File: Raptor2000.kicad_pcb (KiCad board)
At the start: 4 copper layers, 63.5 x 63.5 mm, 35 parts, among them J1 Wuerth_7499010121A, J4 Micro_SD_Card, SW1 SW_Push, U1 TM4C1294NCPDTGOOD, U2 ET60T-02-24-02-X-RTX-GP, U4 ESP-12E, U5 IS42S16400J-xC, Y1 Crystal_GND24

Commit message: updates
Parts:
- removed C17, C18: C_Small, Capacitor_SMD:C_0603_1608Metric
- removed J1: Wuerth_7499010121A, Connector_RJ:RJ45_Wuerth_7499010121A_Horizontal
- removed R3, R36, R4: R_Small, Resistor_SMD:R_0603_1608Metric
- removed SW1: SW_Push, Button_Switch_SMD:SW_SPST_EVPBF
- removed U4: ESP-12E, RF_Module:ESP-12E
- added R5: R_Small, Resistor_SMD:R_0603_1608Metric, F.Cu at (159.3, 94.5)
- U2: footprint Exodus_Connectors:ET60T-02-24-02-X-RTX-GP-HS -> ET60T-02-24-02-X-RTX-GP:ET60T-02-24-02-X-RTX-GP
- moved J4 52.3 mm to (135.9, 71.6), turned to 180 degrees
- moved D1 52.1 mm to (183.6, 66.8)
- moved R30 48.8 mm to (183.6, 68.6), turned to 0 degrees
- moved C1 35.3 mm to (145.7, 111.4), turned to 0 degrees
- moved C7 34.9 mm to (137.4, 104.9), turned to 270 degrees
- moved C2 33.5 mm to (149.4, 111.4), turned to 0 degrees
- moved C9 33.0 mm to (139.2, 104.9), turned to 270 degrees
- moved C6 32.5 mm to (153.7, 111.5), turned to 0 degrees
- moved C38 32.2 mm to (170.1, 70.7), turned to 0 degrees
- moved C5 32.0 mm to (137.4, 101.6), turned to 90 degrees
- moved C35 30.4 mm to (177.0, 81.8), turned to 270 degrees
- moved C10 30.0 mm to (139.2, 101.6), turned to 270 degrees
- moved C36 28.7 mm to (165.5, 70.7), turned to 0 degrees
- moved C8 23.1 mm to (158.5, 104.8), turned to 90 degrees
- moved C33 22.6 mm to (171.8, 90.3), turned to 0 degrees
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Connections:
- D1 pad 2: +BATT -> +3V3
- U1 pad 102: Net-(U1-Pad102) -> (no net)
- U1 pad 105: Net-(U1-Pad105) -> (no net)
- U1 pad 106: Net-(U1-Pad106) -> (no net)
- U1 pad 107: Net-(U1-Pad107) -> (no net)
- U1 pad 108: Net-(U1-Pad108) -> (no net)
- U1 pad 109: Net-(U1-Pad109) -> (no net)
- U1 pad 11: Net-(U1-Pad11) -> (no net)
- U1 pad 110: Net-(U1-Pad110) -> (no net)
- U1 pad 111: Net-(U1-Pad111) -> (no net)
- U1 pad 112: Net-(U1-Pad112) -> (no net)
- U1 pad 116: Net-(U1-Pad116) -> (no net)
- U1 pad 117: Net-(U1-Pad117) -> (no net)
- U1 pad 118: Net-(U1-Pad118) -> (no net)
- U1 pad 119: Net-(U1-Pad119) -> (no net)
- U1 pad 12: Net-(U1-Pad12) -> (no net)
- U1 pad 120: Net-(U1-Pad120) -> (no net)
- U1 pad 121: Net-(U1-Pad121) -> (no net)
- U1 pad 123: Net-(U1-Pad123) -> (no net)
- U1 pad 124: Net-(U1-Pad124) -> (no net)
- U1 pad 125: Net-(U1-Pad125) -> (no net)
- U1 pad 126: Net-(U1-Pad126) -> (no net)
- U1 pad 13: Net-(U1-Pad13) -> (no net)
- U1 pad 14: Net-(U1-Pad14) -> (no net)
- U1 pad 15: Net-(U1-Pad15) -> (no net)
- U1 pad 27: Net-(U1-Pad27) -> (no net)
- U1 pad 29: Net-(U1-Pad29) -> (no net)
- U1 pad 30: Net-(U1-Pad30) -> (no net)
- U1 pad 31: Net-(U1-Pad31) -> /Connectors/~ENABLE
- U1 pad 32: Net-(U1-Pad32) -> /Connectors/~INHIBIT
- U1 pad 33: Net-(U1-Pad33) -> (no net)
- U1 pad 34: Net-(U1-Pad34) -> (no net)
- U1 pad 35: Net-(U1-Pad35) -> (no net)
- U1 pad 36: Net-(U1-Pad36) -> (no net)
- U1 pad 37: Net-(U1-Pad37) -> (no net)
- U1 pad 38: Net-(U1-Pad38) -> (no net)
- U1 pad 42: /Connectors/ETH_LED0 -> (no net)
- U1 pad 43: Net-(U1-Pad43) -> (no net)
- U1 pad 44: Net-(U1-Pad44) -> (no net)
- U1 pad 45: Net-(U1-Pad45) -> (no net)
- U1 pad 46: /Connectors/ETH_LED1 -> (no net)
- U1 pad 5: Net-(U1-Pad5) -> (no net)
- U1 pad 6: Net-(U1-Pad6) -> (no net)
- U1 pad 60: Net-(U1-Pad60) -> (no net)
- U1 pad 61: Net-(U1-Pad61) -> (no net)
- U1 pad 63: Net-(U1-Pad63) -> (no net)
- U1 pad 64: Net-(U1-Pad64) -> (no net)
- U1 pad 65: Net-(U1-Pad65) -> (no net)
- U1 pad 66: Net-(U1-Pad66) -> (no net)
- U1 pad 67: Net-(U1-Pad67) -> (no net)
- U1 pad 71: Net-(U1-Pad71) -> (no net)
- U1 pad 72: Net-(U1-Pad72) -> (no net)
- U1 pad 73: Net-(U1-Pad73) -> (no net)
- U1 pad 74: Net-(U1-Pad74) -> (no net)
- U1 pad 85: Net-(U1-Pad85) -> (no net)
- U1 pad 86: Net-(U1-Pad86) -> (no net)
- U1 pad 91: Net-(U1-Pad91) -> (no net)
- U1 pad 95: /TM4C129/USB_ID -> (no net)
- U1 pad 96: Net-(U1-Pad96) -> (no net)
- U2 pad 1: Net-(U2-Pad1) -> (no net)
- U2 pad 10: /Connectors/BOARD_SENSE -> (no net)
- U2 pad 11: /Connectors/~SYSRESET -> /JTAG_TDO
- U2 pad 12: Net-(U2-Pad12) -> /JTAG_TDI
- U2 pad 13: Net-(U2-Pad13) -> (no net)
- U2 pad 14: Net-(U2-Pad14) -> (no net)
- U2 pad 15: Net-(U2-Pad15) -> (no net)
- U2 pad 19: /JTAG_TDO -> /JTAG_TMS
- U2 pad 2: Net-(U2-Pad2) -> (no net)
- U2 pad 20: /JTAG_TDI -> /JTAG_TCK
- U2 pad 21: /JTAG_TMS -> /TM4C129/ETH_RXI_N
- U2 pad 22: /JTAG_TCK -> /TM4C129/ETH_RXI_P
- U2 pad 23: /Connectors/~JTAG_TRST -> /TM4C129/ETH_TXO_N
- U2 pad 24: Net-(U2-Pad24) -> /TM4C129/ETH_TXO_P
- U2 pad 3: Net-(U2-Pad3) -> (no net)
- U2 pad 4: Net-(U2-Pad4) -> (no net)
- U2 pad 5: Net-(U2-Pad5) -> (no net)
- U2 pad 6: Net-(U2-Pad6) -> (no net)
- U2 pad 7: Net-(U2-Pad7) -> (no net)
- U2 pad 9: Net-(U2-Pad9) -> (no net)
- U5 pad 40: Net-(U5-Pad40) -> (no net)
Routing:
- net /TM4C129/USB_D_N: track 0.00 -> 58.2 mm
- net /TM4C129/USB_D_P: track 0.00 -> 58.2 mm
- net /JTAG_TDO: track 0.00 -> 48.0 mm, vias 0 -> 1
- net /JTAG_TDI: track 0.00 -> 47.5 mm, vias 0 -> 1
- net /JTAG_TCK: track 0.00 -> 42.5 mm, vias 0 -> 1
- net /JTAG_TMS: track 0.00 -> 41.6 mm, vias 0 -> 1
- net /Connectors/SPI_SS: track 12.4 -> 53.7 mm
- net /Connectors/SPI_SCLK: track 14.4 -> 54.9 mm
- net /Connectors/SPI_MOSI: track 16.9 -> 52.2 mm
- net /Connectors/SPI_MISO: track 18.1 -> 51.1 mm
- net /Connectors/SPI_DAT2: track 14.6 -> 47.4 mm
- net /Connectors/SPI_DAT3: track 16.7 -> 46.7 mm
- net /TM4C129/ETH_TXO_P: track 0.00 -> 27.9 mm
- net /TM4C129/ETH_TXO_N: track 0.00 -> 27.5 mm
- net +BATT: track 0.00 -> 26.0 mm
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- added copper zone on In2.Cu, net +3V3
- removed copper zone on B.Cu, net +3V3
- removed copper zone on In2.Cu, net +BATT
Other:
- net class Default: clearance 0.2 -> 0.127; trace_width 0.25 -> 0.1778
- rule trace_clearance: 0.2 -> 0.127

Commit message: fixing some unnamed nets.
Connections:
- net Net-(C4-Pad2) renamed /TM4C129/OSC1_R
- net Net-(C5-Pad1) renamed /TM4C129/VDDC
- net Net-(D1-Pad1) renamed /PWR_LED_CATHODE
- net Net-(R2-Pad1) renamed /TM4C129/R_BIAS
- net Net-(R5-Pad2) renamed /TM4C129/RST

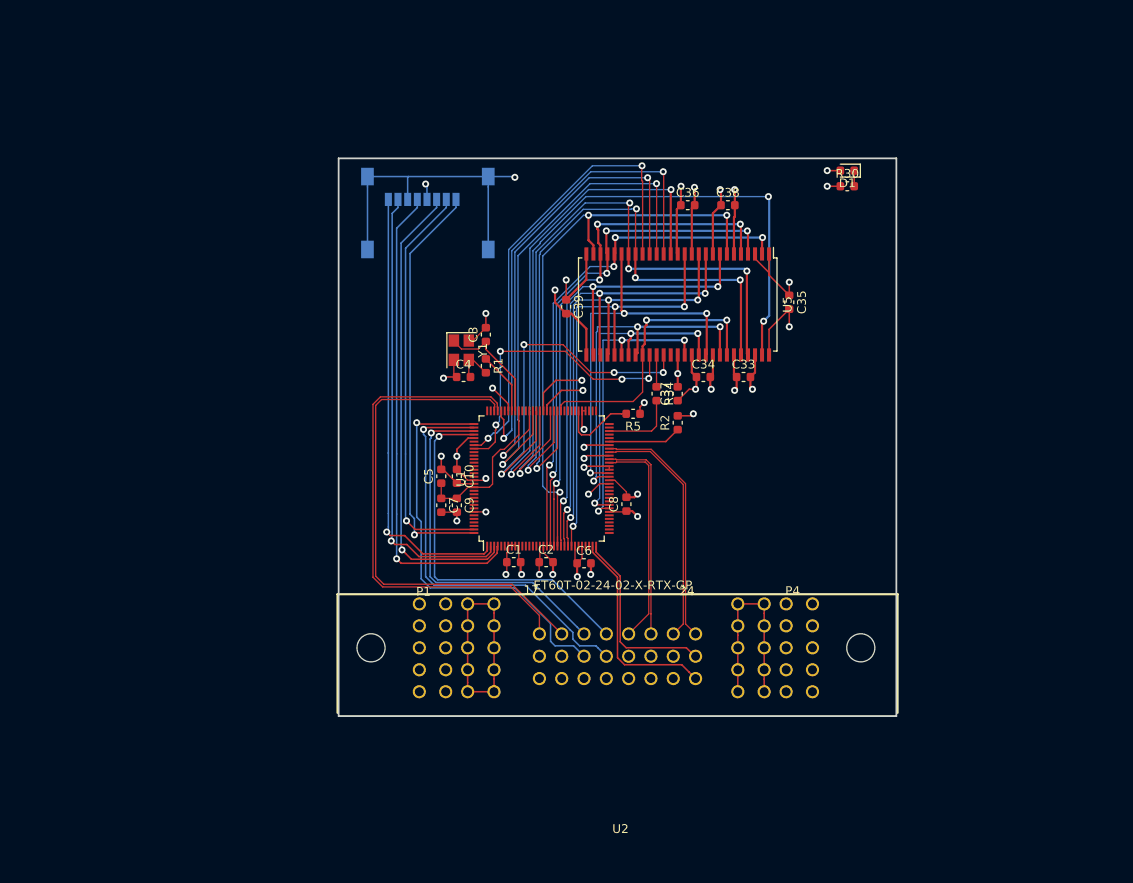
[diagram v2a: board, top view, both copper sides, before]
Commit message: regenerated netlist/annotations and refdeses. using new connector symbol.
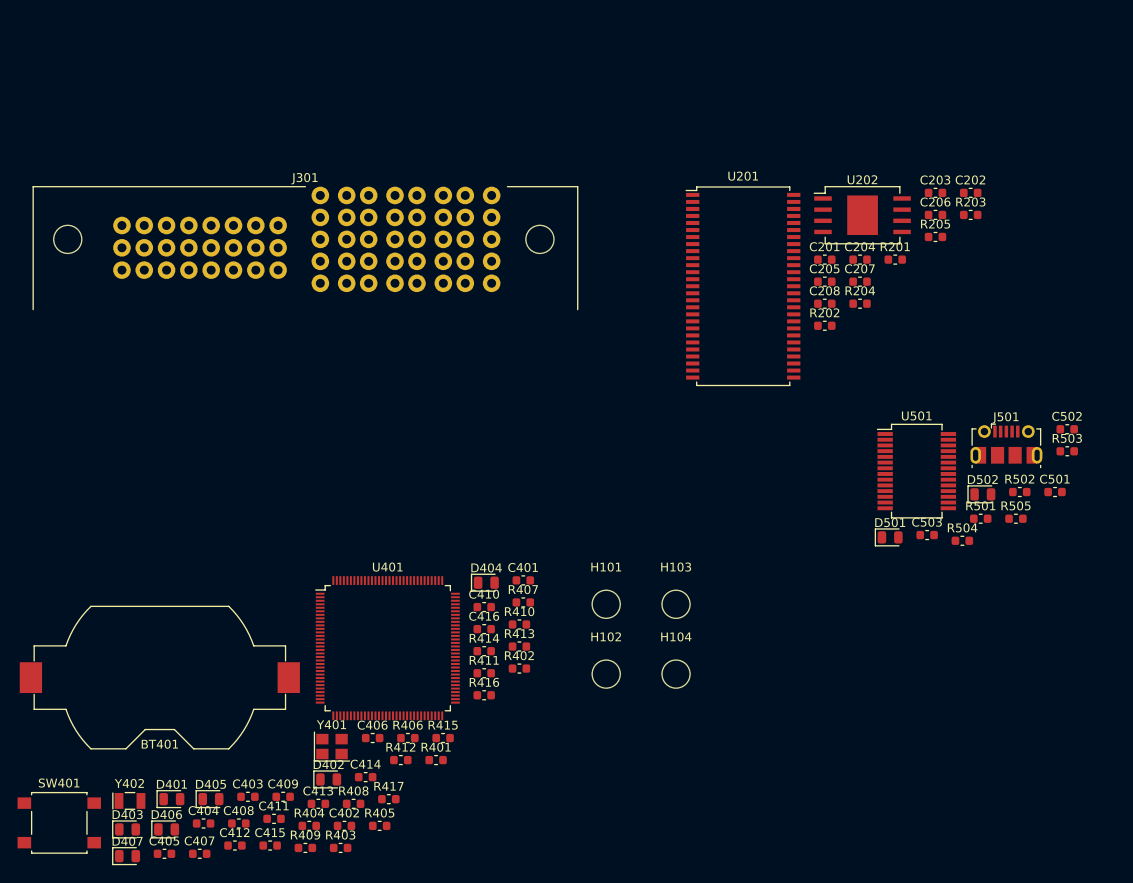
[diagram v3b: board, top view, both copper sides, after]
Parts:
- removed C1, C9: 2.2u, Capacitor_SMD:C_0603_1608Metric
- removed C10, C33, C34, C35, C36, C37, C38, C39, C7: C_Small, Capacitor_SMD:C_0603_1608Metric
- removed C2, C6, C8: 0.1u, Capacitor_SMD:C_0603_1608Metric
- removed C3, C4: 12p, Capacitor_SMD:C_0603_1608Metric
- removed C5: 1.0u, Capacitor_SMD:C_0603_1608Metric
- removed D1: LED, LED_SMD:LED_0603_1608Metric
- removed J4: Micro_SD_Card, Connector_Card:microSD_HC_Wuerth_693072010801
- removed R1: 2k, Resistor_SMD:R_0603_1608Metric
- removed R2: 4.87k 1%, Resistor_SMD:R_0603_1608Metric
- removed R30, R5: R_Small, Resistor_SMD:R_0603_1608Metric
- removed R34: 0, Resistor_SMD:R_0603_1608Metric
- removed U1: TM4C1294NCPDTGOOD, Package_QFP:TQFP-128_14x14mm_P0.4mm
- removed U2: ET60T-02-24-02-X-RTX-GP, ET60T-02-24-02-X-RTX-GP:ET60T-02-24-02-X-RTX-GP
- removed U5: IS42S16400J-xC, Package_SO:TSOP-II-54_22.2x10.16mm_P0.8mm
- removed Y1: Crystal_GND24, Crystal:Crystal_SMD_3225-4Pin_3.2x2.5mm
- added BT401: Battery_Cell, Battery:BatteryHolder_Keystone_1058_1x2032, F.Cu at (105.4, 124.5)
- added C201: 0.1u, Capacitor_SMD:C_0603_1608Metric, F.Cu at (181.1, 76.9)
- added C202: 0.1u, Capacitor_SMD:C_0603_1608Metric, F.Cu at (197.7, 69.3)
- added C203: 0.1u, Capacitor_SMD:C_0603_1608Metric, F.Cu at (193.7, 69.3)
- added C204: 0.1u, Capacitor_SMD:C_0603_1608Metric, F.Cu at (185.1, 76.9)
- added C205: 0.1u, Capacitor_SMD:C_0603_1608Metric, F.Cu at (181.1, 79.4)
- added C206: 0.1u, Capacitor_SMD:C_0603_1608Metric, F.Cu at (193.7, 71.8)
- added C207: 0.1u, Capacitor_SMD:C_0603_1608Metric, F.Cu at (185.1, 79.4)
- added C208: 0.1u, Capacitor_SMD:C_0603_1608Metric, F.Cu at (181.1, 82.0)
- added C401: 12p, Capacitor_SMD:C_0603_1608Metric, F.Cu at (146.8, 113.5)
- added C402: 12p, Capacitor_SMD:C_0603_1608Metric, F.Cu at (126.4, 141.4)
- added C403: 0.1u, Capacitor_SMD:C_0603_1608Metric, F.Cu at (115.4, 138.1)
- added C404: 1.0u, Capacitor_SMD:C_0603_1608Metric, F.Cu at (110.4, 141.1)
- added C405: 0.1u, Capacitor_SMD:C_0603_1608Metric, F.Cu at (105.9, 144.6)
- added C406: 0.1u, Capacitor_SMD:C_0603_1608Metric, F.Cu at (129.6, 131.4)
- added C407: 0.1u, Capacitor_SMD:C_0603_1608Metric, F.Cu at (109.9, 144.6)
- added C408: 2.2u, Capacitor_SMD:C_0603_1608Metric, F.Cu at (114.4, 141.1)
- added C409: 0.1u, Capacitor_SMD:C_0603_1608Metric, F.Cu at (119.4, 138.1)
- added C410: 0.1u, Capacitor_SMD:C_0603_1608Metric, F.Cu at (142.3, 116.5)
- added C411: 12p, Capacitor_SMD:C_0603_1608Metric, F.Cu at (118.4, 140.6)
- added C412: 12p, Capacitor_SMD:C_0603_1608Metric, F.Cu at (113.9, 143.6)
- added C413: 0.1u, Capacitor_SMD:C_0603_1608Metric, F.Cu at (123.4, 138.9)
- added C414: 0.1u, Capacitor_SMD:C_0603_1608Metric, F.Cu at (128.8, 135.9)
- added C415: 0.1u, Capacitor_SMD:C_0603_1608Metric, F.Cu at (117.9, 143.6)
- added C416: 2.2u, Capacitor_SMD:C_0603_1608Metric, F.Cu at (142.3, 119.0)
- added C501: 0.1u, Capacitor_SMD:C_0603_1608Metric, F.Cu at (207.3, 103.4)
- added C502: 100nF, Capacitor_SMD:C_0603_1608Metric, F.Cu at (208.7, 96.2)
- added C503: 3300pF, Capacitor_SMD:C_0603_1608Metric, F.Cu at (192.7, 108.3)
- added D401: LED, LED_SMD:LED_0805_2012Metric, F.Cu at (106.7, 138.4)
- added D402: LED, LED_SMD:LED_0805_2012Metric, F.Cu at (124.6, 136.1)
- added D403: LED, LED_SMD:LED_0805_2012Metric, F.Cu at (101.7, 141.8)
- added D404: LED, LED_SMD:LED_0805_2012Metric, F.Cu at (142.5, 113.7)
- added D405: LED, LED_SMD:LED_0805_2012Metric, F.Cu at (111.2, 138.4)
- added D406: LED, LED_SMD:LED_0805_2012Metric, F.Cu at (106.1, 141.8)
- added D407: LED, LED_SMD:LED_0805_2012Metric, F.Cu at (101.7, 144.9)
- added D501: LED, Diode_SMD:D_0805_2012Metric, F.Cu at (188.5, 108.6)
- added D502: LED, Diode_SMD:D_0805_2012Metric, F.Cu at (199.1, 103.7)
- added H101: MountingHole, MountingHole:MountingHole_3.2mm_M3, F.Cu at (156.2, 116.2)
- added H102: MountingHole, MountingHole:MountingHole_3.2mm_M3, F.Cu at (156.2, 124.1)
- added H103: MountingHole, MountingHole:MountingHole_3.2mm_M3, F.Cu at (164.1, 116.2)
- added H104: MountingHole, MountingHole:MountingHole_3.2mm_M3, F.Cu at (164.1, 124.1)
- added J301: ET60T-000-3-08-D04-x-R1-S-x, Exodus_Connectors:Conn_Samtec_ET60T-000-3-08-D-4-x-R1-S-x, F.Cu at (122.0, 74.6)
- added J501: USB_B_Micro, Connector_USB:USB_Micro-B_Molex-105017-0001, F.Cu at (201.8, 98.0)
- added R201: 0, Resistor_SMD:R_0603_1608Metric, F.Cu at (189.1, 76.9)
- added R202: DNP, Resistor_SMD:R_0603_1608Metric, F.Cu at (181.1, 84.5)
- added R203: 1M, Resistor_SMD:R_0603_1608Metric, F.Cu at (197.7, 71.8)
- added R204: DNP, Resistor_SMD:R_0603_1608Metric, F.Cu at (185.1, 82.0)
- added R205: 10k, Resistor_SMD:R_0603_1608Metric, F.Cu at (193.7, 74.4)
- added R401: 51, Resistor_SMD:R_0603_1608Metric, F.Cu at (136.8, 133.9)
- added R402: 100, Resistor_SMD:R_0603_1608Metric, F.Cu at (146.3, 123.5)
- added R403: 2k, Resistor_SMD:R_0603_1608Metric, F.Cu at (126.0, 143.9)
- added R404: 4.87k 1%, Resistor_SMD:R_0603_1608Metric, F.Cu at (122.4, 141.4)
- added R405: 10k, Resistor_SMD:R_0603_1608Metric, F.Cu at (130.4, 141.4)
- added R406: 100, Resistor_SMD:R_0603_1608Metric, F.Cu at (133.6, 131.4)
- added R407: 330, Resistor_SMD:R_0603_1608Metric, F.Cu at (146.8, 116.0)
- added R408: 330, Resistor_SMD:R_0603_1608Metric, F.Cu at (127.4, 138.9)
- added R409: 49.9, Resistor_SMD:R_0603_1608Metric, F.Cu at (121.9, 143.9)
- added R410: 49.9, Resistor_SMD:R_0603_1608Metric, F.Cu at (146.3, 118.5)
- added R411: 49.9, Resistor_SMD:R_0603_1608Metric, F.Cu at (142.3, 124.0)
- added R412: 49.9, Resistor_SMD:R_0603_1608Metric, F.Cu at (132.8, 133.9)
- added R413: 330, Resistor_SMD:R_0603_1608Metric, F.Cu at (146.3, 121.0)
- added R414: 330, Resistor_SMD:R_0603_1608Metric, F.Cu at (142.3, 121.5)
- added R415: 330, Resistor_SMD:R_0603_1608Metric, F.Cu at (137.6, 131.4)
- added R416: 330, Resistor_SMD:R_0603_1608Metric, F.Cu at (142.3, 126.5)
- added R417: 330, Resistor_SMD:R_0603_1608Metric, F.Cu at (131.4, 138.4)
- added R501: 330, Resistor_SMD:R_0603_1608Metric, F.Cu at (198.8, 106.4)
- added R502: 330, Resistor_SMD:R_0603_1608Metric, F.Cu at (203.3, 103.4)
- added R503: 4.7k, Resistor_SMD:R_0603_1608Metric, F.Cu at (208.7, 98.8)
- added R504: 10k, Resistor_SMD:R_0603_1608Metric, F.Cu at (196.7, 108.9)
- added R505: 1M, Resistor_SMD:R_0603_1608Metric, F.Cu at (202.8, 106.4)
- added SW401: RST_SW, Button_Switch_SMD:SW_SPST_B3S-1000, F.Cu at (93.9, 141.1)
- added U201: IS42S16400J-xC, Package_SO:TSOP-II-54_22.2x10.16mm_P0.8mm, F.Cu at (171.8, 80.0)
- added U202: TC58CVG2S0HRAIG, Exodus_Packages:WSON-8-1EP_3.4x4.3mm_P1.27mm, F.Cu at (185.4, 71.9)
- added U401: TM4C1294NCPDTGOOD, Package_QFP:TQFP-128_14x14mm_P0.4mm, F.Cu at (131.3, 121.2)
- added U501: FT232RL, Package_SO:SSOP-28_5.3x10.2mm_P0.65mm, F.Cu at (191.6, 101.0)
- added Y401: Crystal_GND24, Crystal:Crystal_SMD_3225-4Pin_3.2x2.5mm, F.Cu at (125.0, 132.4)
- added Y402: Crystal, Crystal:Crystal_SMD_MicroCrystal_CC7V-T1A-2Pin_3.2x1.5mm, F.Cu at (102.0, 138.6)
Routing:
- net GND: track 126.4 -> 0.00 mm, vias 21 -> 0
- net +3V3: track 94.7 -> 0.00 mm, vias 21 -> 0
- net /Memory/EPIOS15: track 82.4 -> 0.00 mm, vias 3 -> 0
- net /Memory/EPIOS14: track 76.9 -> 0.00 mm, vias 4 -> 0
- net /Memory/EPIOS13: track 73.8 -> 0.00 mm, vias 4 -> 0
- net /Memory/EPIOS3: track 68.1 -> 0.00 mm, vias 3 -> 0
- net /Memory/EPIOS16: track 61.5 -> 0.00 mm, vias 2 -> 0
- net /Memory/EPIOS2: track 60.0 -> 0.00 mm, vias 4 -> 0
- net /Memory/EPIOS18: track 59.3 -> 0.00 mm, vias 2 -> 0
- net /Memory/EPIOS1: track 58.9 -> 0.00 mm, vias 4 -> 0
- net /Memory/EPIOS0: track 58.6 -> 0.00 mm, vias 4 -> 0
- net /TM4C129/USB_D_N: track 58.2 -> 0.00 mm
- net /TM4C129/USB_D_P: track 58.2 -> 0.00 mm
- net /Memory/EPIOS4: track 57.6 -> 0.00 mm, vias 3 -> 0
- net /Memory/EPIOS19: track 57.4 -> 0.00 mm, vias 2 -> 0
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- removed copper zone on In2.Cu, net +3V3
- removed copper zone on In1.Cu, net GND
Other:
- board outline removed

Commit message: started layout. fixing some netnames.
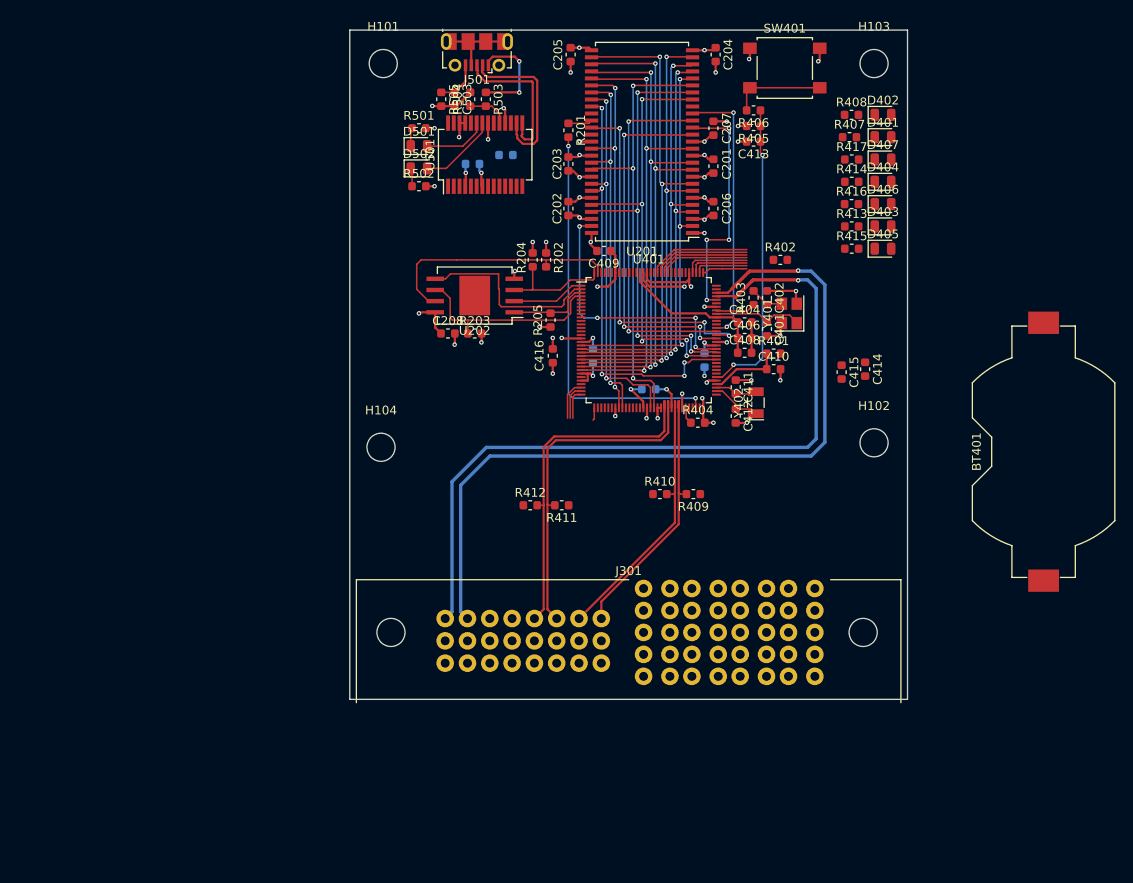
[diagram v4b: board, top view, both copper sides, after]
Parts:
- C403, C405, C407, C501, C502: moved to B.Cu
- moved SW401 119.2 mm to (176.5, 55.1)
- moved D407 117.0 mm to (187.7, 65.5)
- moved D401 110.6 mm to (187.7, 63.0)
- moved D403 110.1 mm to (187.7, 73.2)
- moved D406 108.3 mm to (187.7, 70.6)
- moved BT401 103.9 mm to (206.0, 98.8), turned to 270 degrees
- moved D405 98.9 mm to (187.7, 75.7)
- moved D402 98.5 mm to (187.7, 60.5)
- moved R408 96.8 mm to (184.1, 60.5)
- moved R405 90.3 mm to (173.0, 61.7), turned to 180 degrees
- moved C413 90.2 mm to (173.0, 63.5), turned to 180 degrees
- moved R417 89.9 mm to (184.2, 65.5)
- moved C415 84.5 mm to (183.0, 89.7), turned to 270 degrees
- moved Y402 84.5 mm to (173.2, 93.2), turned to 90 degrees
- moved C404 84.0 mm to (172.0, 84.1)
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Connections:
- net Net-(C503-Pad1) renamed /USB_to_UART/DBG_USB_SHIELD
- net Net-(J501-Pad1) renamed /USB_to_UART/DBG_VBUS
- net Net-(J501-Pad2) renamed /USB_to_UART/DBG_USB_D_N
- net Net-(J501-Pad3) renamed /USB_to_UART/DBG_USB_D_P
- C404 pad 1: +3V3 -> /TM4C129/VDDC
- C406 pad 1: +3V3 -> /TM4C129/VDDC
- C408 pad 1: +3V3 -> /TM4C129/VDDC
- D404 pad 1: /TM4C129/USER_LED1_CATHOD -> /TM4C129/USER_LED2_CATHODE
- D406 pad 1: /TM4C129/USER_LED0_CATHODE -> /TM4C129/USER_LED1_CATHODE
- D407 pad 1: /TM4C129/USER_LED1_CATHOD -> /TM4C129/USER_LED3_CATHODE
- R414 pad 2: /TM4C129/USER_LED1_CATHOD -> /TM4C129/USER_LED2_CATHODE
- R416 pad 2: /TM4C129/USER_LED0_CATHODE -> /TM4C129/USER_LED1_CATHODE
- R417 pad 2: /TM4C129/USER_LED1_CATHOD -> /TM4C129/USER_LED3_CATHODE
- U401 pad 115: Net-(U401-Pad115) -> /TM4C129/VDDC
- U401 pad 87: Net-(U401-Pad115) -> /TM4C129/VDDC
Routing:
- net /TM4C129/USB_D_P: track 0.00 -> 91.0 mm, vias 0 -> 1
- net GND: track 0.00 -> 90.9 mm, vias 0 -> 37
- net /TM4C129/USB_D_N: track 0.00 -> 89.3 mm, vias 0 -> 1
- net +3V3: track 0.00 -> 63.9 mm, vias 0 -> 25
- net /Memory/EPI0S4: track 0.00 -> 55.2 mm, vias 0 -> 3
- net /Memory/EPI0S5: track 0.00 -> 54.5 mm, vias 0 -> 3
- net /Memory/EPI0S6: track 0.00 -> 53.1 mm, vias 0 -> 3
- net /Memory/EPI0S7: track 0.00 -> 52.1 mm, vias 0 -> 3
- net /Memory/EPI0S10: track 0.00 -> 50.3 mm, vias 0 -> 3
- net /Memory/EPI0S3: track 0.00 -> 50.1 mm, vias 0 -> 3
- net /Memory/EPI0S14: track 0.00 -> 50.0 mm, vias 0 -> 5
- net /Memory/EPI0S13: track 0.00 -> 49.5 mm, vias 0 -> 5
- net /Memory/EPI0S2: track 0.00 -> 47.9 mm, vias 0 -> 3
- net /Memory/EPI0S12: track 0.00 -> 47.6 mm, vias 0 -> 5
- net /Memory/EPI0S1: track 0.00 -> 46.1 mm, vias 0 -> 3
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- added copper zone on In2.Cu, net +3V3
- added copper zone on In1.Cu, net GND
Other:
- board outline added: 63.5 x 76.2 mm
- net class Default: via_dia 0.8 -> 0.508; via_drill 0.4 -> 0.254
- net class Ethernet added: clearance 0.127, trace_width 0.1778, via_dia 0.508, via_drill 0.254
- net class Memory added: clearance 0.127, trace_width 0.1778, via_dia 0.508, via_drill 0.254
- net class Power added: clearance 0.127, trace_width 0.254, via_dia 0.508, via_drill 0.254
- net class USB added: clearance 0.127, trace_width 0.254, via_dia 0.508, via_drill 0.254
- rule pad_to_mask_clearance: 0.051 -> 0.0508
- rule via_min_size: 0.508 -> 0.4572
